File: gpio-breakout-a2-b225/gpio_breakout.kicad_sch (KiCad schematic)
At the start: 9 parts, among them J1 ZF5S-40-01-T-WT-K-TR, J2 Pi GPIO 2x20

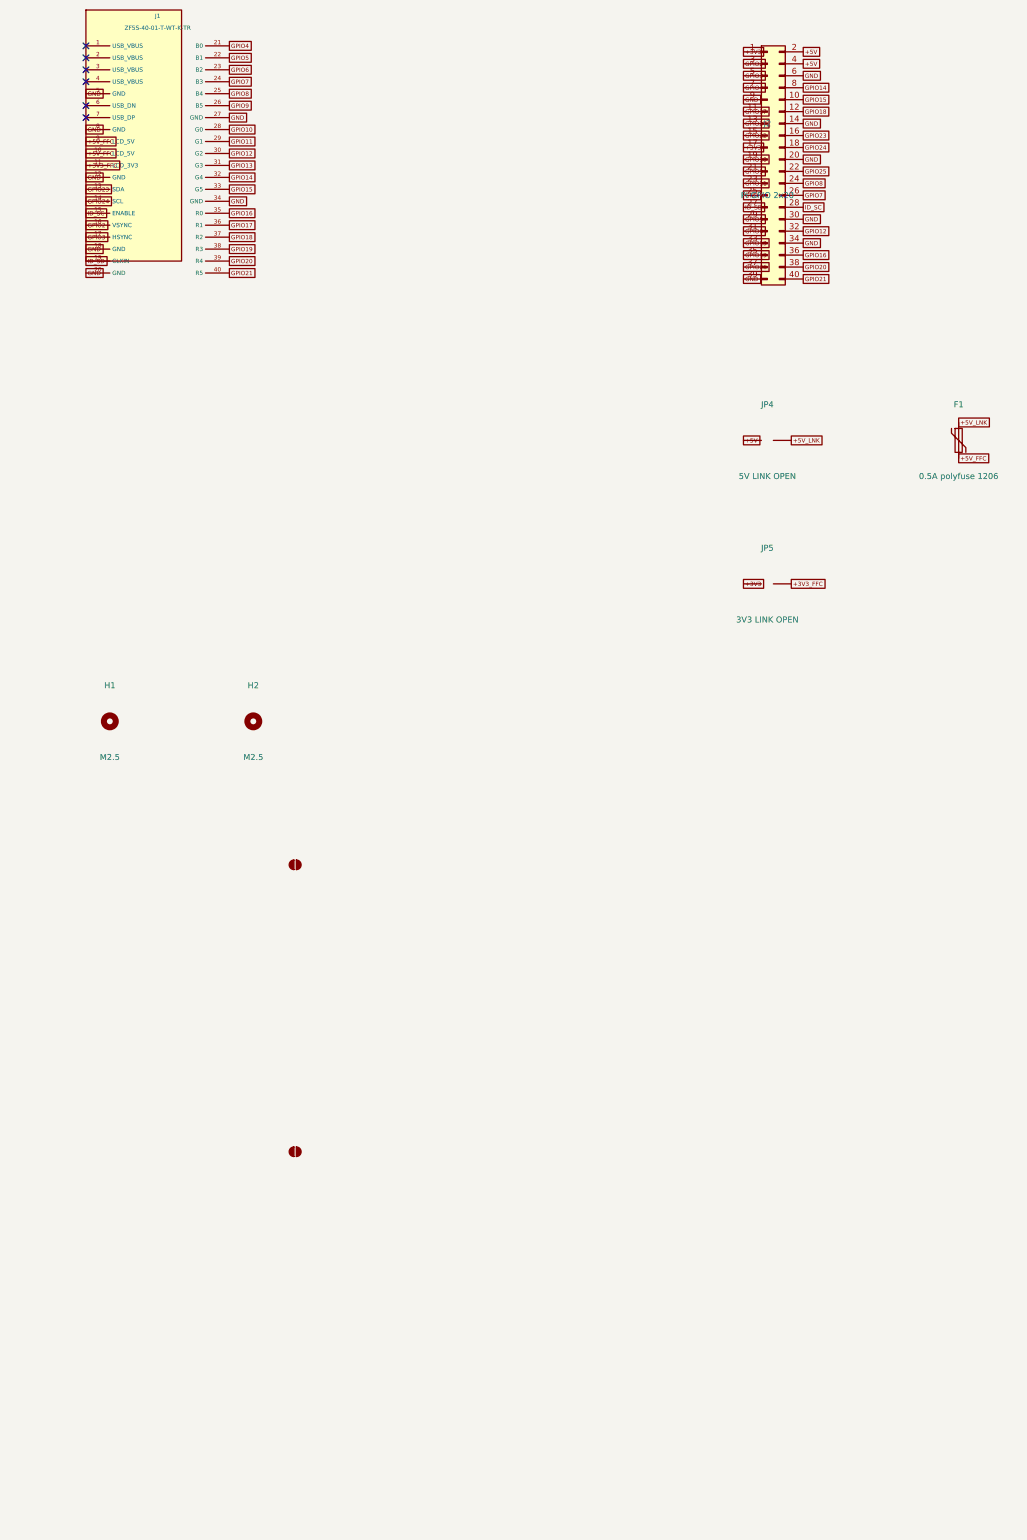
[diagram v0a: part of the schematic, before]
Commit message: Add protected USB2 input to B2.25 GPIO LCD addon
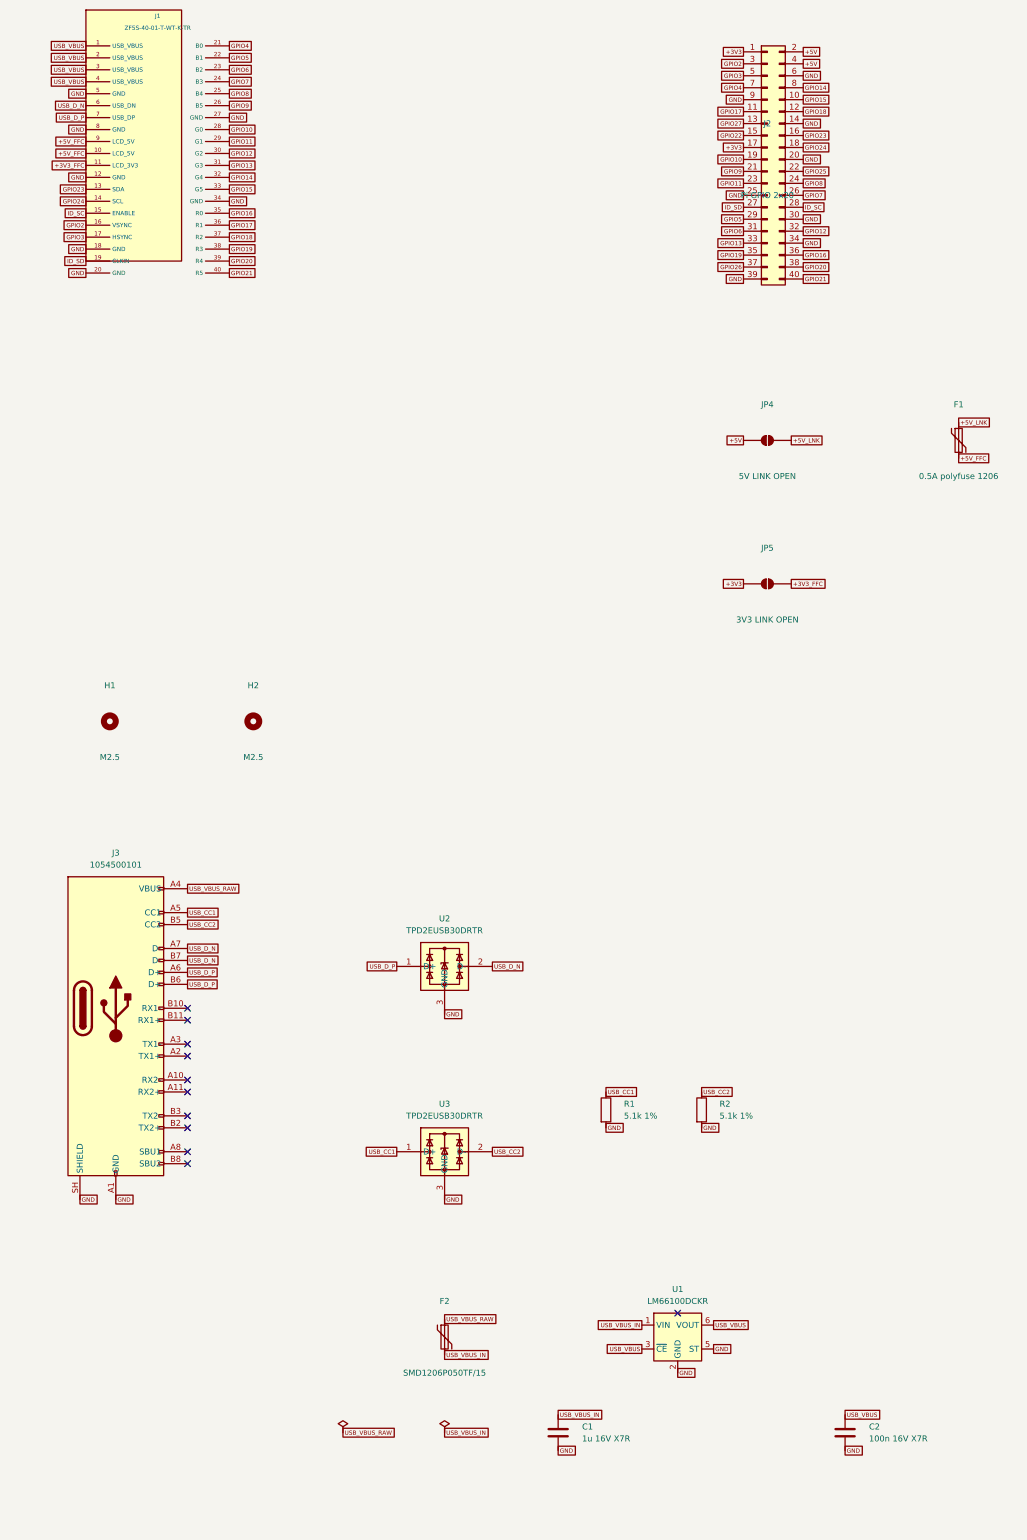
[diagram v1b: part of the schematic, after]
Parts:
- added C1: 1u 16V X7R, Capacitor_SMD:C_0603_1608Metric, symbol Device:C
- added C2: 100n 16V X7R, Capacitor_SMD:C_0603_1608Metric, symbol Device:C
- added F2: SMD1206P050TF/15, Fuse:Fuse_1206_3216Metric, symbol Device:Polyfuse
- added J3: 1054500101, USB_A2:USB_C_Receptacle_Molex_105450-0101, symbol Connector:USB_C_Receptacle
- added R1, R2: 5.1k 1%, Resistor_SMD:R_0603_1608Metric, symbol Device:R
- added U1: LM66100DCKR, Package_TO_SOT_SMD:SOT-363_SC-70-6, symbol Power_Management:LM66100DCK
- added U2, U3: TPD2EUSB30DRTR, Package_TO_SOT_SMD:Texas_DRT-3, symbol Power_Protection:TPD2EUSB30
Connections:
- net GND: now also C1.2, C2.2, J3.A1 (GND), J3.A12 (GND), J3.B1 (GND), J3.B12 (GND), J3.SH (SHIELD), R1.2, R2.2, U1.2 (GND), U1.5 (ST), U2.3 (GND), U3.3 (GND)
- net USB_VBUS: now reaches J1.1 (USB_VBUS)
- net USB_VBUS: now also J1.2 (USB_VBUS), J1.3 (USB_VBUS), J1.4 (USB_VBUS), C2.1, U1.3 (~{CE}), U1.6 (VOUT)
- net USB_D_N: now reaches J1.6 (USB_DN)
- net USB_D_N: now also J3.A7 (D-), J3.B7 (D-), U2.2 (D-)
- net USB_D_P: now reaches J1.7 (USB_DP)
- net USB_D_P: now also J3.A6 (D+), J3.B6 (D+), U2.1 (D+)
- new net USB_CC1: J3.A5 (CC1), R1.1, U3.1 (D+)
- new net USB_CC2: J3.B5 (CC2), R2.1, U3.2 (D-)
- new net USB_VBUS_IN: C1.1, F2.2, U1.1 (VIN)
- new net USB_VBUS_RAW: F2.1, J3.A4 (VBUS), J3.A9 (VBUS), J3.B4 (VBUS), J3.B9 (VBUS)
- no-connect marks 6 -> 11
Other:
- title: GPIO LCD bench adapter -> GPIO LCD A2 - B2.25 interface with USB2 host input
- moved on the sheet: JP4, JP5

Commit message: Add GPIO A2 USB soft start and Pi-side display series provisions
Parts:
- added C3: 10n 50V C0G 5%, Capacitor_SMD:C_0603_1608Metric, symbol Device:C
- added C4: 1u 16V X7R, Capacitor_SMD:C_0603_1608Metric, symbol Device:C
- added RN1, RN2, RN3, RN4, RN5, RN6: 0R x4 (DPI source option), Resistor_SMD:R_Array_Convex_4x0603, symbol Device:R_Pack04
- added U4: TPS22918DBVR, Package_TO_SOT_SMD:SOT-23-6, symbol GPIO_Qualification:TPS22918DBV
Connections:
- net GND: now also C3.2, C4.2, U4.2 (GND)
- net GPIO10: now also RN3.8 (R1.2); no longer J2.19 (Pin_19)
- net GPIO11: now also RN3.6 (R3.2); no longer J2.23 (Pin_23)
- net GPIO12: now also RN5.6 (R3.2); no longer J2.32 (Pin_32)
- net GPIO13: now also RN5.5 (R4.2); no longer J2.33 (Pin_33)
- net GPIO14: now also RN1.5 (R4.2); no longer J2.8 (Pin_8)
- net GPIO15: now also RN2.8 (R1.2); no longer J2.10 (Pin_10)
- net GPIO16: now also RN6.7 (R2.2); no longer J2.36 (Pin_36)
- net GPIO17: now also RN2.7 (R2.2); no longer J2.11 (Pin_11)
- net GPIO18: now also RN2.6 (R3.2); no longer J2.12 (Pin_12)
- net GPIO19: now also RN6.8 (R1.2); no longer J2.35 (Pin_35)
- net GPIO2: now also RN1.8 (R1.2); no longer J2.3 (Pin_3)
- net GPIO20: now also RN6.6 (R3.2); no longer J2.38 (Pin_38)
- net GPIO21: now also RN6.5 (R4.2); no longer J2.40 (Pin_40)
- net GPIO3: now also RN1.7 (R2.2); no longer J2.5 (Pin_5)
- net GPIO4: now also RN1.6 (R3.2); no longer J2.7 (Pin_7)
- net GPIO5: now also RN5.8 (R1.2); no longer J2.29 (Pin_29)
- net GPIO6: now also RN5.7 (R2.2); no longer J2.31 (Pin_31)
- net GPIO7: now also RN4.8 (R1.2); no longer J2.26 (Pin_26)
- net GPIO8: now also RN3.5 (R4.2); no longer J2.24 (Pin_24)
- net GPIO9: now also RN3.7 (R2.2); no longer J2.21 (Pin_21)
- net ID_SC: now also RN4.6 (R3.2); no longer J2.28 (Pin_28)
- net ID_SD: now also RN4.7 (R2.2); no longer J2.27 (Pin_27)
- net USB_VBUS_IN: now also U4.1 (VIN), U4.3 (ON); no longer U1.1 (VIN)
- new net GPIO10_PI: J2.19 (Pin_19), RN3.1 (R1.1)
- new net GPIO11_PI: J2.23 (Pin_23), RN3.3 (R3.1)
- new net GPIO12_PI: J2.32 (Pin_32), RN5.3 (R3.1)
- new net GPIO13_PI: J2.33 (Pin_33), RN5.4 (R4.1)
- new net GPIO14_PI: J2.8 (Pin_8), RN1.4 (R4.1)
- new net GPIO15_PI: J2.10 (Pin_10), RN2.1 (R1.1)
- new net GPIO16_PI: J2.36 (Pin_36), RN6.2 (R2.1)
- new net GPIO17_PI: J2.11 (Pin_11), RN2.2 (R2.1)
- new net GPIO18_PI: J2.12 (Pin_12), RN2.3 (R3.1)
- new net GPIO19_PI: J2.35 (Pin_35), RN6.1 (R1.1)
- new net GPIO20_PI: J2.38 (Pin_38), RN6.3 (R3.1)
- new net GPIO21_PI: J2.40 (Pin_40), RN6.4 (R4.1)
- new net GPIO2_PI: J2.3 (Pin_3), RN1.1 (R1.1)
- new net GPIO3_PI: J2.5 (Pin_5), RN1.2 (R2.1)
- new net GPIO4_PI: J2.7 (Pin_7), RN1.3 (R3.1)
- new net GPIO5_PI: J2.29 (Pin_29), RN5.1 (R1.1)
- new net GPIO6_PI: J2.31 (Pin_31), RN5.2 (R2.1)
- new net GPIO7_PI: J2.26 (Pin_26), RN4.1 (R1.1)
- new net GPIO8_PI: J2.24 (Pin_24), RN3.4 (R4.1)
- new net GPIO9_PI: J2.21 (Pin_21), RN3.2 (R2.1)
- new net ID_SC_PI: J2.28 (Pin_28), RN4.3 (R3.1)
- new net ID_SD_PI: J2.27 (Pin_27), RN4.2 (R2.1)
- new net USB_SLEW_CT: C3.1, U4.4 (CT)
- new net USB_VBUS_SOFT: C4.1, U1.1 (VIN), U4.6 (VOUT)
- no-connect marks 11 -> 16
